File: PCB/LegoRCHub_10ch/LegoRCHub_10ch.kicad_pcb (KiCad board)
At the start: 2 copper layers, 39.3 x 55.2 mm, 41 parts, among them J1 Conn_01x02, J10 Conn_01x03, J11 Conn_01x03_MountingPin, J12 Conn_01x02, J13 Conn_01x01, J2 Conn_01x02, J3 Conn_01x02, J4 Conn_01x02, J5 Conn_01x02, J6 Conn_01x02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

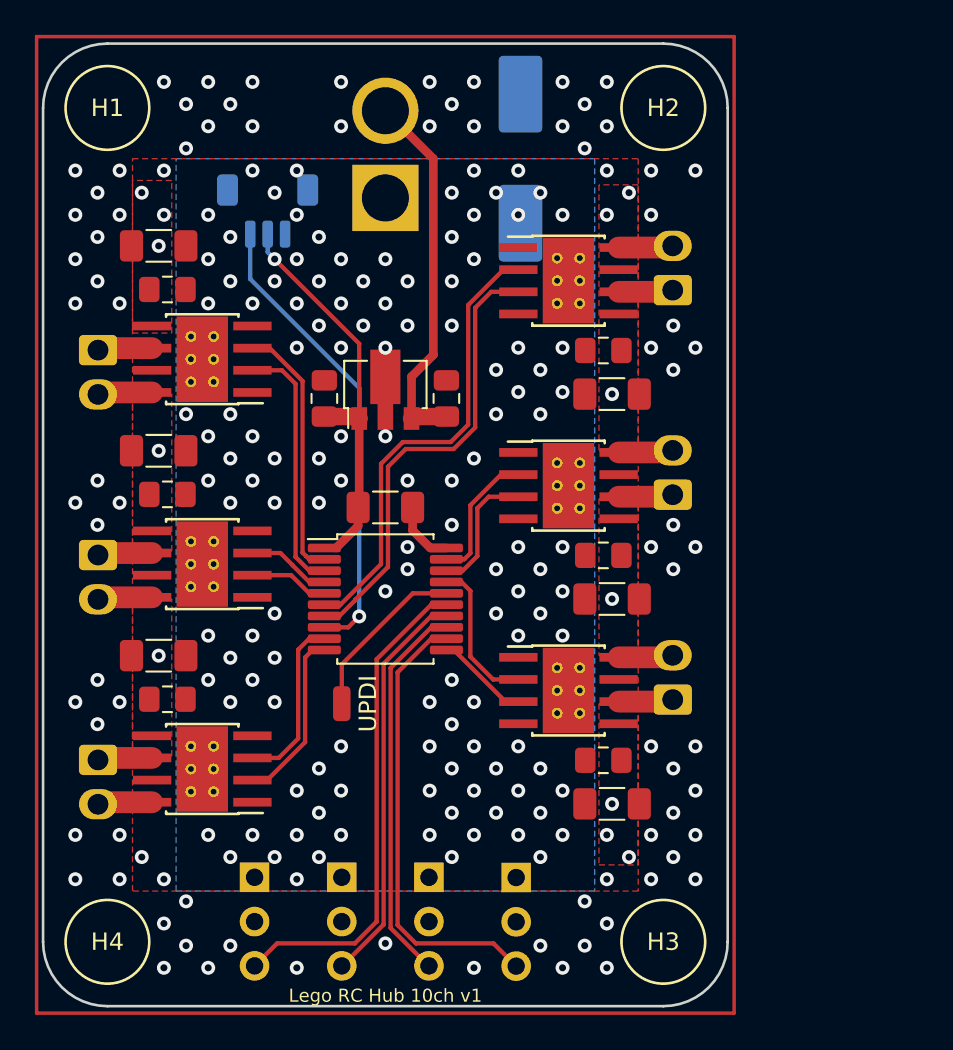
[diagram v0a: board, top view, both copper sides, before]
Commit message: Lego RC Hub 10ch v2: fully migrated to KiCad8
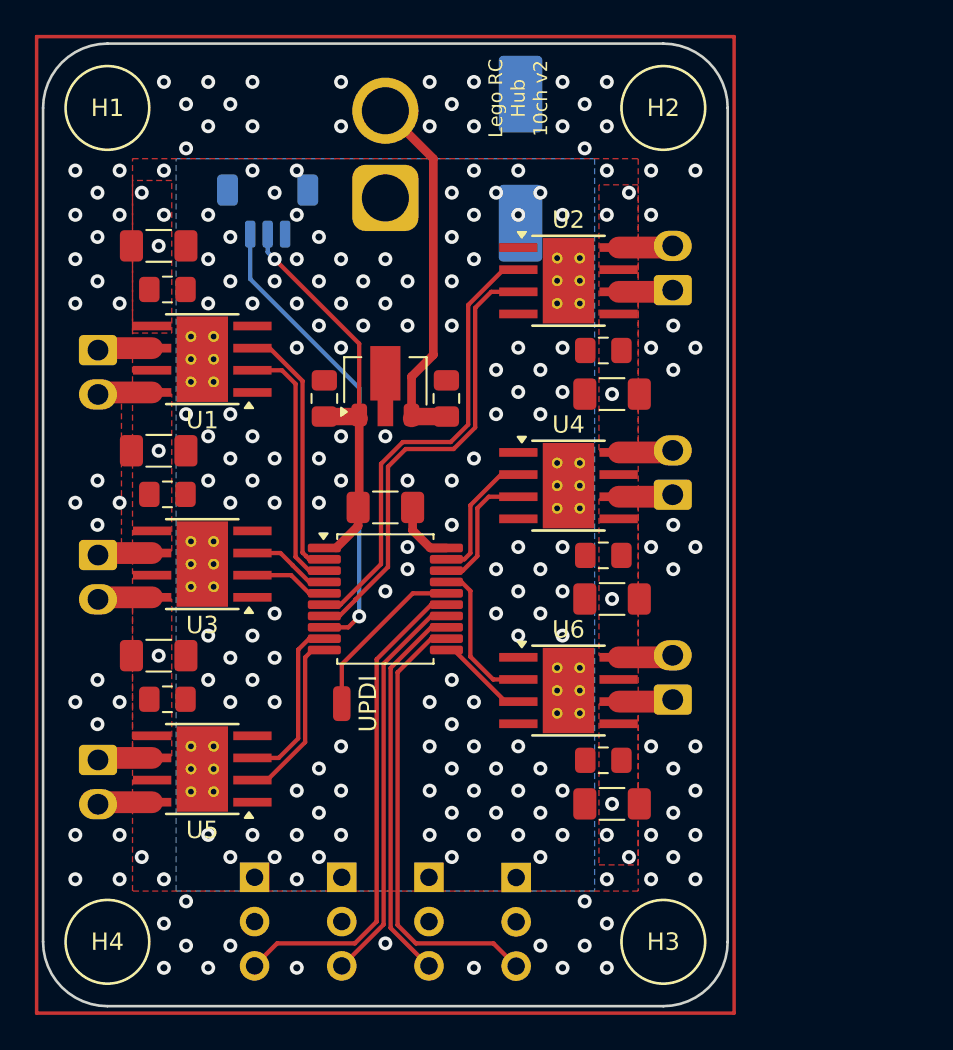
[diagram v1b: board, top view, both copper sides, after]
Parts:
- U1, U2, U3, U4, U5, U6: footprint Package_SO:Texas_HTSOP-8-1EP_3.9x4.9mm_P1.27mm_EP2.95x4.9mm_Mask2.4x3.1mm_ThermalVias -> CustomFootprints:Texas_HTSOP-8-1EP_3.9x4.9mm_P1.27mm_EP2.95x4.9mm_Mask2.4x3.1mm_ThermalVias
- moved U8 0.50 mm to (44.5, 42.5)
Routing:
- net GND: vias 124 -> 123
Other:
- board text added: "Lego RC Hub 10ch v2"
- board text removed: "Lego RC Hub 10ch v1"

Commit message: Lego RC Hub 10ch v3: improved zones
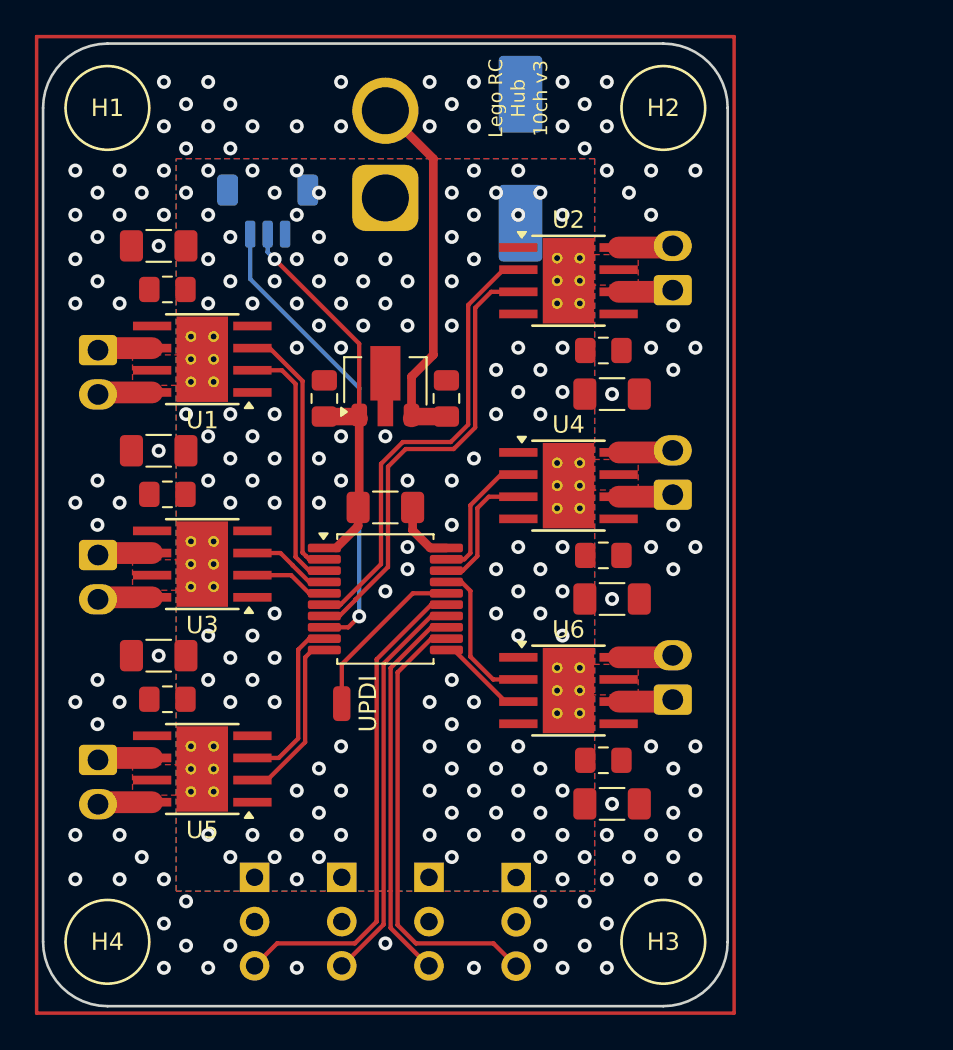
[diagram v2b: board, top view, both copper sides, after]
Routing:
- net GND: vias 123 -> 125
- net +BATT: vias 96 -> 102
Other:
- board text added: "Lego RC Hub 10ch v3"
- board text removed: "Lego RC Hub 10ch v2"
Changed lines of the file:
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@@
 	(paper "A4")
 	(title_block
-		(title "Lego RC Hub 10ch v2")
+		(title "Lego RC Hub 10ch v3")
 	)
 	(layers
@@
 		)
 	)
-	(gr_text "Lego RC \nHub \n10ch v2"
+	(gr_text "Lego RC \nHub \n10ch v3"
 		(at 52.07 26.33869 90)
 		(layer "F.SilkS")
@@
 	)
 	(via
+		(at 38.1 44.45)
+		(size 0.8)
+		(drill 0.4)
+		(layers "F.Cu" "B.Cu")
+		(free yes)
+		(net 1)
+	)
+	(via
 		(at 39.37 38.1)
 		(size 0.8)
@@
 	)
 	(via
+		(at 40.64 31.75)
+		(size 0.8)
+		(drill 0.4)
+		(layers "F.Cu" "B.Cu")
+		(free yes)
+		(net 1)
+	)
+	(via
 		(at 52.07 40.64)
 		(size 0.8)
@@
 	)
 	(via
+		(at 54.61 71.12)
+		(size 0.8)
+		(drill 0.4)
+		(layers "F.Cu" "B.Cu")
+		(free yes)
+		(net 2)
+	)
+	(via
 		(at 31.75 30.48)
 		(size 0.8)
@@
 	)
 	(via
+		(at 53.34 72.39)
+		(size 0.8)
+		(drill 0.4)
+		(layers "F.Cu" "B.Cu")
+		(free yes)
+		(net 2)
+	)
+	(via
 		(at 26.67 71.12)
 		(size 0.8)
@@
 	)
 	(via
+		(at 39.37 27.94)
+		(size 0.8)
+		(drill 0.4)
+		(layers "F.Cu" "B.Cu")
+		(free yes)
+		(net 2)
+	)
+	(via
 		(at 58.42 31.75)
 		(size 0.8)
@@
 	)
 	(via
+		(at 35.56 29.21)
+		(size 0.8)
+		(drill 0.4)
+		(layers "F.Cu" "B.Cu")
+		(free yes)
+		(net 2)
+	)
+	(via
 		(at 59.69 40.64)
 		(size 0.8)
@@
 	)
 	(via
+		(at 55.88 69.85)
+		(size 0.8)
+		(drill 0.4)
+		(layers "F.Cu" "B.Cu")
+		(free yes)
+		(net 2)
+	)
+	(via
 		(at 30.48 69.85)
 		(size 0.8)
@@
 	)
 	(via
-		(at 57.15 33.02)
+		(at 57.15 73.66)
 		(size 0.8)
 		(drill 0.4)
@@
 	)
 	(via
-		(at 57.15 73.66)
+		(at 33.02 26.67)
 		(size 0.8)
 		(drill 0.4)
@@
 	)
 	(via
-		(at 33.02 26.67)
+		(at 62.23 66.04)
 		(size 0.8)
 		(drill 0.4)
@@
 	)
 	(via
-		(at 62.23 66.04)
+		(at 26.67 35.56)
 		(size 0.8)
 		(drill 0.4)
@@
 	)
 	(via
-		(at 26.67 35.56)
+		(at 31.75 27.94)
 		(size 0.8)
 		(drill 0.4)
@@
 	)
 	(via
+		(at 34.29 30.48)
+		(size 0.8)
+		(drill 0.4)
+		(layers "F.Cu" "B.Cu")
+		(free yes)
+		(net 2)
+	)
+	(via
 		(at 55.88 72.39)
 		(size 0.8)
@@
 	)
 	(via
-		(at 54.61 27.94)
+		(at 33.02 31.75)
 		(size 0.8)
 		(drill 0.4)
@@
 	)
 	(via
-		(at 36.83 25.4)
+		(at 54.61 27.94)
 		(size 0.8)
 		(drill 0.4)
@@
 	)
 	(zone
-		(net 2)
-		(net_name "+BATT")
-		(layer "F.Cu")
-		(hatch edge 0.508)
-		(priority 2)
-		(connect_pads yes
-			(clearance 0.254)
-		)
-		(min_thickness 0.254)
-		(filled_areas_thickness no)
-		(fill yes
-			(thermal_gap 0.508)
-			(thermal_bridge_width 0.508)
-			(smoothing fillet)
-			(radius 0.5)
-			(island_removal_mode 1)
-			(island_area_min 0)
-		)
-		(polygon
-			(pts
-				(xy 58.95 61.05) (xy 56.7 61.05) (xy 56.7 70.3) (xy 58.95 70.3)
-			)
-		)
-	)
-	(zone
 		(net 1)
 		(net_name "GND")
@@
 			(thermal_gap 0.508)
 			(thermal_bridge_width 0.508)
-			(smoothing chamfer)
-			(radius 4)
 			(island_removal_mode 1)
 			(island_area_min 0)
@@
 		(polygon
 			(pts
-				(xy 29.95 29.8) (xy 58.95 29.8) (xy 58.95 71.8) (xy 29.95 71.8)
+				(xy 58.95 35.3) (xy 56.2 35.3) (xy 56.2 37.05) (xy 58.95 37.05)
 			)
 		)
 	)
 	(zone
-		(net 2)
-		(net_name "+BATT")
+		(net 1)
+		(net_name "GND")
 		(layer "F.Cu")
 		(hatch edge 0.508)
-		(priority 2)
+		(priority 1)
 		(connect_pads yes
 			(clearance 0.254)
@@
 			(thermal_gap 0.508)
 			(thermal_bridge_width 0.508)
-			(smoothing fillet)
-			(radius 0.5)
 			(island_removal_mode 1)
 			(island_area_min 0)
@@
 		(polygon
 			(pts
-				(xy 58.95 31.3) (xy 56.7 31.3) (xy 56.7 46.55) (xy 58.95 46.55)
+				(xy 29.95 54.55) (xy 32.7 54.549999) (xy 32.699999 52.8) (xy 29.95 52.8)
 			)
 		)
 	)
 	(zone
-		(net 2)
-		(net_name "+BATT")
+		(net 1)
+		(net_name "GND")
 		(layer "F.Cu")
 		(hatch edge 0.508)
-		(priority 2)
+		(priority 1)
 		(connect_pads yes
 			(clearance 0.254)
@@
 			(thermal_gap 0.508)
 			(thermal_bridge_width 0.508)
-			(smoothing fillet)
-			(radius 0.5)
 			(island_removal_mode 1)
 			(island_area_min 0)
@@
 		(polygon
 			(pts
-				(xy 32.2 55.05) (xy 29.95 55.05) (xy 29.95 64.05) (xy 32.2 64.05)
+				(xy 58.95 58.8) (xy 56.2 58.8) (xy 56.2 60.55) (xy 58.95 60.55)
 			)
 		)
 	)
 	(zone
-		(net 2)
-		(net_name "+BATT")
+		(net 1)
+		(net_name "GND")
 		(layer "F.Cu")
 		(hatch edge 0.508)
-		(priority 2)
+		(priority 1)
 		(connect_pads yes
 			(clearance 0.254)
@@
 			(thermal_gap 0.508)
 			(thermal_bridge_width 0.508)
-			(smoothing fillet)
-			(radius 0.5)
 			(island_removal_mode 1)
 			(island_area_min 0)
@@
 		(polygon
 			(pts
-				(xy 58.95 49.3) (xy 56.7 49.3) (xy 56.7 58.3) (xy 58.95 58.3)
+				(xy 29.95 66.3) (xy 32.7 66.299999) (xy 32.699999 64.55) (xy 29.95 64.55)
 			)
 		)
 	)
 	(zone
-		(net 2)
-		(net_name "+BATT")
+		(net 1)
+		(net_name "GND")
 		(layer "F.Cu")
 		(hatch edge 0.508)
-		(priority 2)
+		(priority 1)
 		(connect_pads yes
 			(clearance 0.254)
@@
 			(thermal_gap 0.508)
 			(thermal_bridge_width 0.508)
-			(smoothing fillet)
-			(radius 0.5)
 			(island_removal_mode 1)
 			(island_area_min 0)
@@
 		(polygon
 			(pts
-				(xy 32.2 31.05) (xy 29.95 31.05) (xy 29.95 39.8) (xy 32.2 39.8)
+				(xy 58.95 47.05) (xy 56.2 47.05) (xy 56.2 48.8) (xy 58.95 48.8)
 			)
 		)
 	)
 	(zone
-		(net 2)
-		(net_name "+BATT")
+		(net 1)
+		(net_name "GND")
 		(layer "F.Cu")
 		(hatch edge 0.508)
-		(priority 2)
+		(priority 1)
 		(connect_pads yes
 			(clearance 0.254)
@@
 			(thermal_gap 0.508)
 			(thermal_bridge_width 0.508)
-			(smoothing fillet)
-			(radius 0.5)
 			(island_removal_mode 1)
 			(island_area_min 0)
@@
 		(polygon
 			(pts
-				(xy 32.2 43.3) (xy 29.315 43.3) (xy 29.315 52.3) (xy 32.2 52.3)
+				(xy 29.95 42.8) (xy 32.7 42.799999) (xy 32.699999 41.05) (xy 29.95 41.05)
 			)
 		)
@@
 			(thermal_gap 0.508)
 			(thermal_bridge_width 0.508)
-			(island_removal_mode 1)
-			(island_area_min 0)
 		)
 		(polygon
@@
 		(net 1)
 		(net_name "GND")
-		(layer "B.Cu")
+		(layers "F&B.Cu")
 		(hatch edge 0.508)
 		(priority 1)

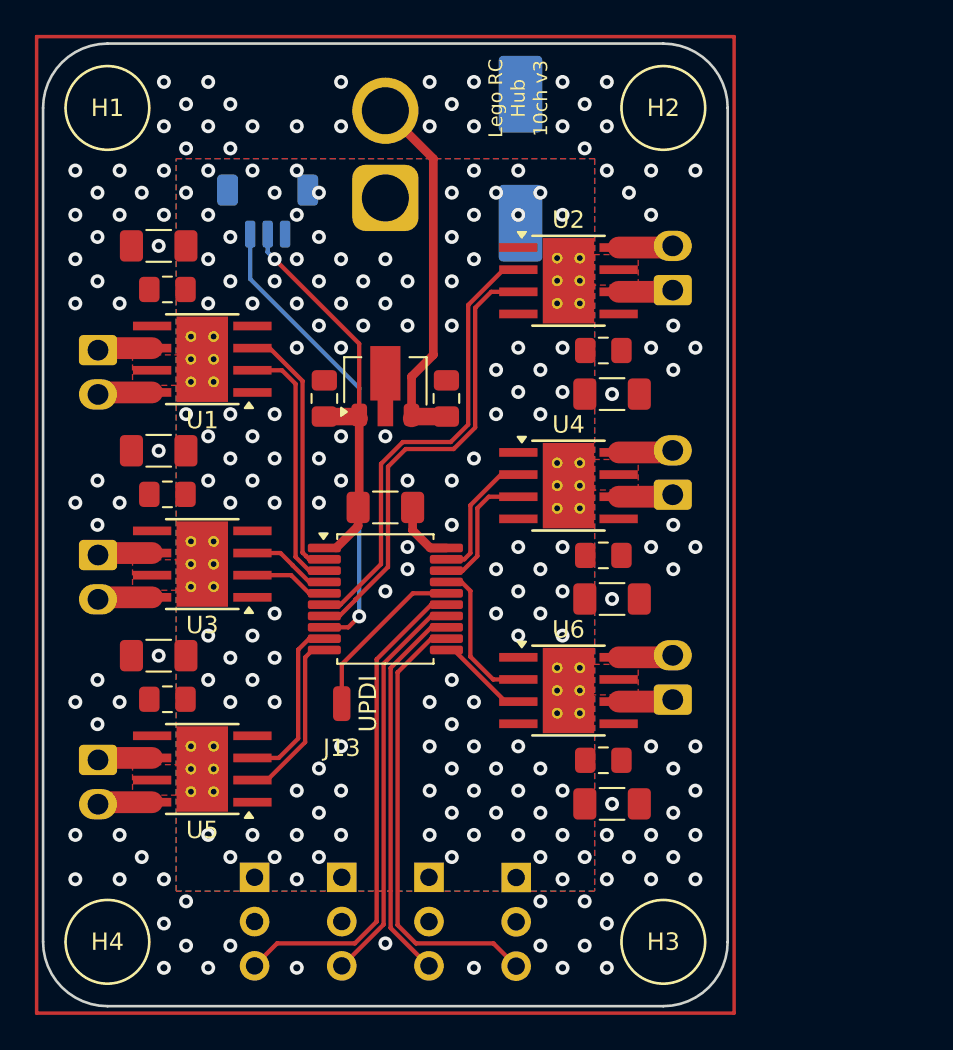
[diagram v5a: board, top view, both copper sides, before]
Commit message: Lego RC Hub 10ch: v5: added additional capacitors on channels + remade all vias
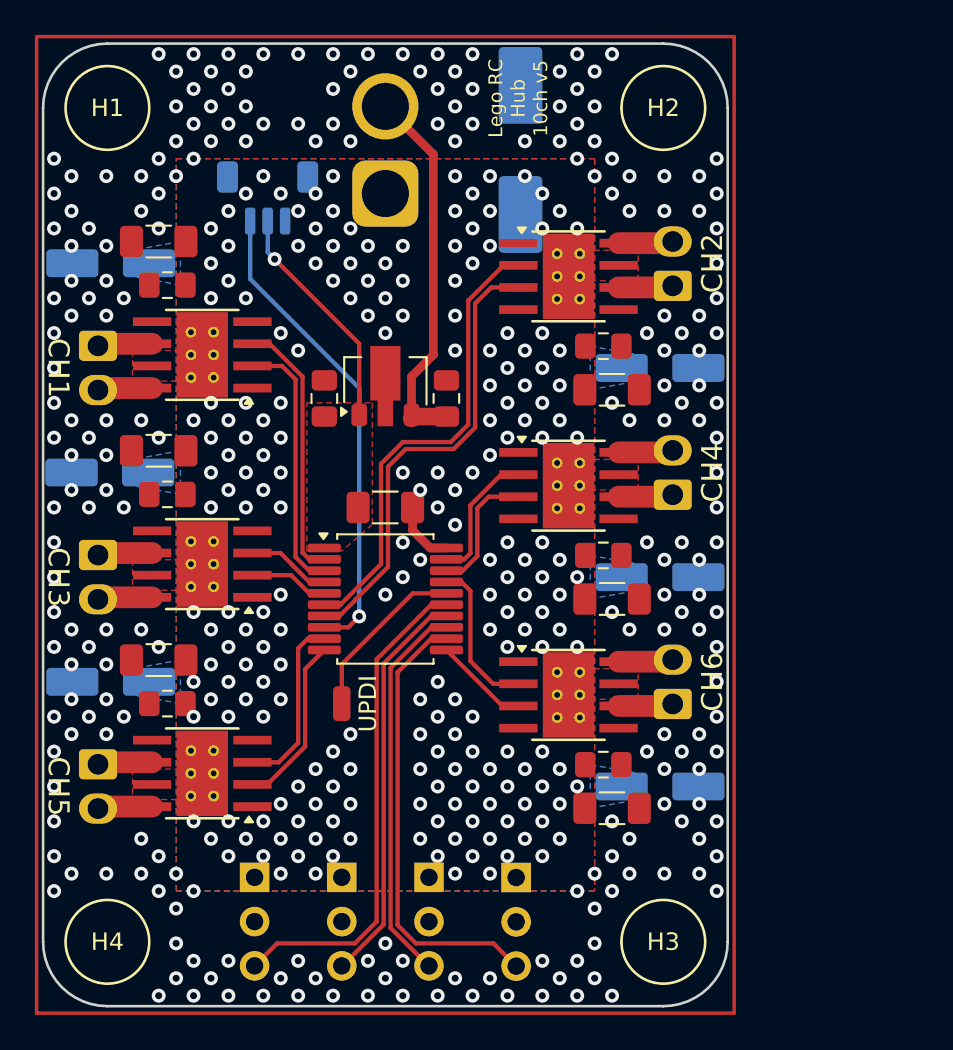
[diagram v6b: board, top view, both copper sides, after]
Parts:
- added C17: 47u, Capacitor_SMD:CP_Elec_5x5.4, B.Cu at (28.7, 35.8)
- added C18: 47u, Capacitor_SMD:CP_Elec_5x5.4, B.Cu at (60.2, 41.8)
- added C19: 47u, Capacitor_SMD:CP_Elec_5x5.4, B.Cu at (28.6, 47.8)
- added C20: 47u, Capacitor_SMD:CP_Elec_5x5.4, B.Cu at (60.2, 53.8)
- added C21: 47u, Capacitor_SMD:CP_Elec_5x5.4, B.Cu at (28.7, 59.8)
- added C22: 47u, Capacitor_SMD:CP_Elec_5x5.4, B.Cu at (60.2, 65.8)
- moved J11 0.75 mm to (37.7, 32.0)
- moved C16 0.50 mm to (52.2, 29.3)
- moved C1 0.25 mm to (31.4, 34.5)
- moved C10 0.25 mm to (31.9, 61.0)
- moved C11 0.25 mm to (57.5, 67.0)
- moved C12 0.25 mm to (57.0, 64.5)
- moved C2 0.25 mm to (31.9, 37.0)
- moved C3 0.25 mm to (57.5, 43.0)
- moved C4 0.25 mm to (57.0, 40.6)
- moved C9 0.25 mm to (31.4, 58.5)
- moved J1 0.25 mm to (28.0, 40.5)
- moved J2 0.25 mm to (60.9, 37.1)
- moved J5 0.25 mm to (28.0, 64.5)
- moved J6 0.25 mm to (60.9, 61.1)
- moved U1 0.25 mm to (34.0, 41.0)
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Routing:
- net VCC: track 22.7 -> 13.5 mm
- net /IBus: track 26.8 -> 27.5 mm
- net /CH5_2: track 8.54 -> 9.07 mm
- net +BATT: track 21.4 -> 21.6 mm, vias 102 -> 226
- net GND: vias 125 -> 205
- added copper zone on F.Cu, net VCC
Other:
- board text added: "HEATSINK"
- board text added: "Lego RC Hub 10ch v5"
- board text removed: "Lego RC Hub 10ch v3"
